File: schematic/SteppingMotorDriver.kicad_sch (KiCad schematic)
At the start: 8 parts

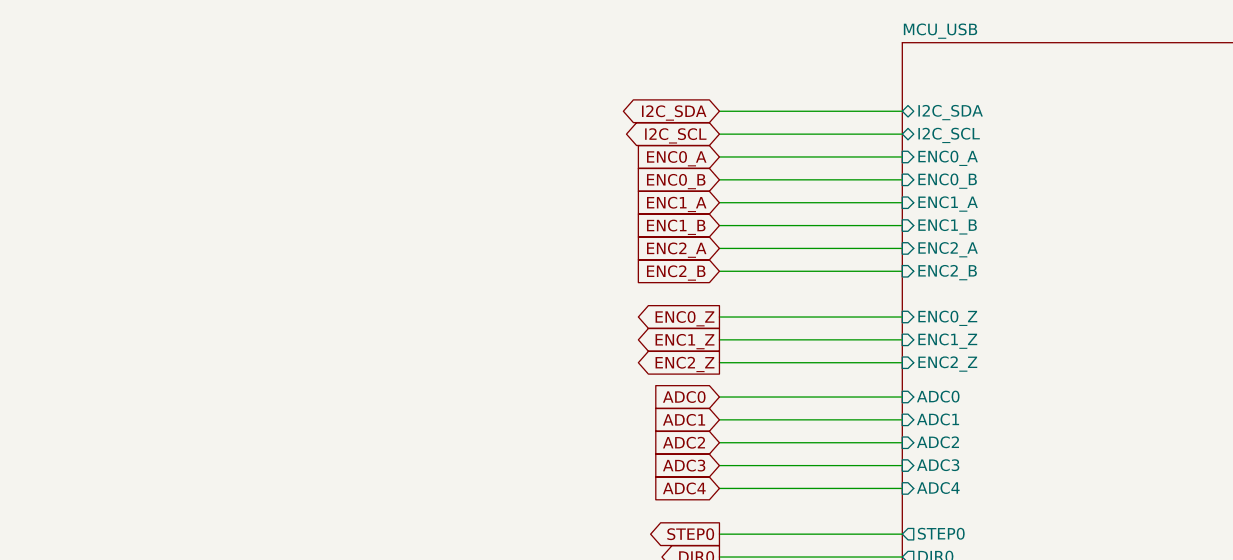
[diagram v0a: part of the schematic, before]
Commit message: Add status LED support, Multiplexer schematic, and Gerber export
Adds status_led.c/h for GPIO46/47 LED indicators, a Multiplexer
schematic sheet, exported Gerber fabrication files, and BLE Codex
prompt docs. Removes stale KiCad auto-backup zips.
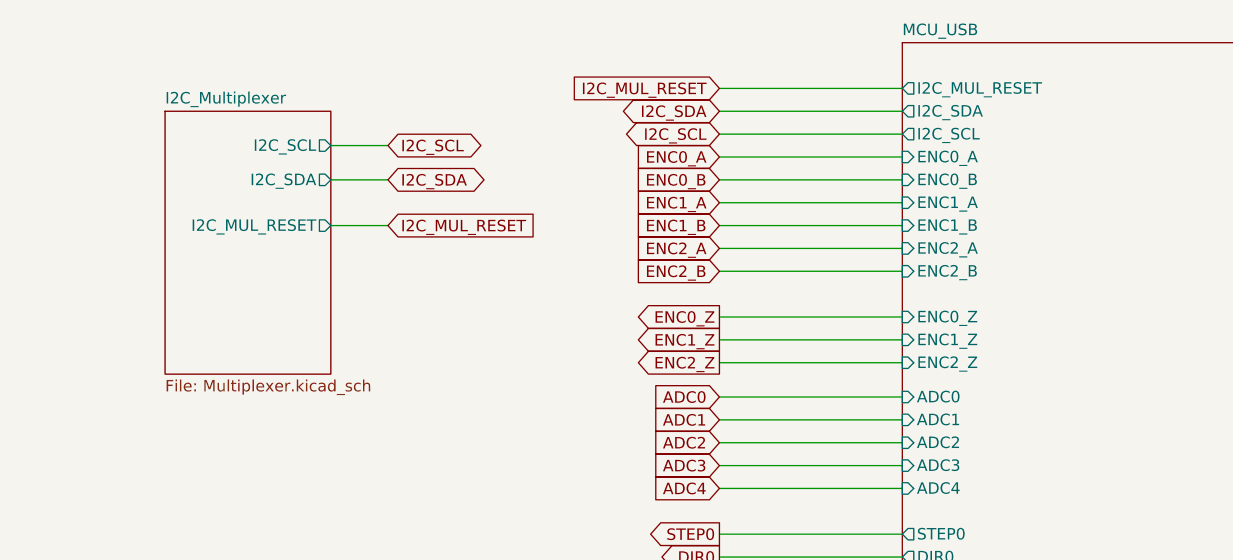
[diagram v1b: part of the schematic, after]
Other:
- added sheet I2C_Multiplexer (Multiplexer.kicad_sch)
- sheet MCU_USB ports: added I2C_MUL_RESET; removed none
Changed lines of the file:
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@@
 	(wire
 		(pts
+			(xy 142.24 31.75) (xy 148.59 31.75)
+		)
+		(stroke
+			(width 0)
+			(type default)
+		)
+	)
+	(wire
+		(pts
 			(xy 201.93 118.11) (xy 217.17 118.11)
 		)
@@
 	(wire
 		(pts
+			(xy 185.42 25.4) (xy 205.74 25.4)
+		)
+		(stroke
+			(width 0)
+			(type default)
+		)
+	)
+	(wire
+		(pts
 			(xy 66.04 62.23) (xy 78.74 62.23)
 		)
@@
 	(wire
 		(pts
+			(xy 142.24 35.56) (xy 148.59 35.56)
+		)
+		(stroke
+			(width 0)
+			(type default)
+		)
+	)
+	(wire
+		(pts
+			(xy 142.24 40.64) (xy 148.59 40.64)
+		)
+		(stroke
+			(width 0)
+			(type default)
+		)
+	)
+	(wire
+		(pts
 			(xy 185.42 33.02) (xy 205.74 33.02)
 		)
@@
 		)
 	)
+	(global_label "I2C_SDA"
+		(shape bidirectional)
+		(at 148.59 35.56 0)
+		(effects
+			(font
+				(size 1.27 1.27)
+			)
+			(justify left)
+		)
+		(property "Intersheetrefs" "${INTERSHEET_REFS}"
+			(at 148.59 35.56 0)
+			(hide yes)
+			(show_name yes)
+			(do_not_autoplace no)
+			(effects
+				(font
+					(size 1.27 1.27)
+				)
+			)
+		)
+	)
+	(global_label "I2C_MUL_RESET"
+		(shape input)
+		(at 148.59 40.64 0)
+		(effects
+			(font
+				(size 1.27 1.27)
+			)
+			(justify left)
+		)
+		(property "Intersheetrefs" "${INTERSHEET_REFS}"
+			(at 148.59 40.64 0)
+			(hide yes)
+			(show_name yes)
+			(do_not_autoplace no)
+			(effects
+				(font
+					(size 1.27 1.27)
+				)
+			)
+		)
+	)
 	(global_label "I2C_SCL"
 		(shape bidirectional)
@@
 		)
 	)
+	(global_label "I2C_MUL_RESET"
+		(shape input)
+		(at 185.42 25.4 180)
+		(effects
+			(font
+				(size 1.27 1.27)
+			)
+			(justify right)
+		)
+		(property "Intersheetrefs" "${INTERSHEET_REFS}"
+			(at 185.42 25.4 0)
+			(hide yes)
+			(show_name yes)
+			(do_not_autoplace no)
+			(effects
+				(font
+					(size 1.27 1.27)
+				)
+			)
+		)
+	)
 	(global_label "ADC1"
 		(shape input)
@@
 		)
 	)
+	(global_label "I2C_SCL"
+		(shape bidirectional)
+		(at 148.59 31.75 0)
+		(effects
+			(font
+				(size 1.27 1.27)
+			)
+			(justify left)
+		)
+		(property "Intersheetrefs" "${INTERSHEET_REFS}"
+			(at 148.59 31.75 0)
+			(hide yes)
+			(show_name yes)
+			(do_not_autoplace no)
+			(effects
+				(font
+					(size 1.27 1.27)
+				)
+			)
+		)
+	)
 	(global_label "ADC1"
 		(shape output)
@@
 			)
 		)
-		(pin "I2C_SDA" bidirectional
+		(pin "I2C_SDA" output
 			(at 205.74 27.94 180)
 			(effects
@@
 			)
 		)
-		(pin "I2C_SCL" bidirectional
+		(pin "I2C_SCL" output
 			(at 205.74 30.48 180)
 			(effects
@@
 			)
 		)
+		(pin "I2C_MUL_RESET" output
+			(at 205.74 25.4 180)
+			(effects
+				(font
+					(size 1.27 1.27)
+				)
+				(justify left)
+			)
+		)
+	)
+	(sheet
+		(at 123.825 27.94)
+		(size 18.415 29.21)
+		(exclude_from_sim no)
+		(in_bom yes)
+		(on_board yes)
+		(dnp no)
+		(fields_autoplaced yes)
+		(stroke
+			(width 0.1524)
+			(type solid)
+		)
+		(fill
+			(color 0 0 0 0)
+		)
+		(property "Sheetname" "I2C_Multiplexer"
+			(at 123.825 27.2284 0)
+			(show_name no)
+			(do_not_autoplace no)
+			(effects
+				(font
+					(size 1.27 1.27)
+				)
+				(justify left bottom)
+			)
+		)
+		(property "Sheetfile" "Multiplexer.kicad_sch"
+			(at 123.825 57.7346 0)
+			(show_name no)
+			(do_not_autoplace no)
+			(effects
+				(font
+					(size 1.27 1.27)
+				)
+				(justify left top)
+			)
+		)
+		(pin "I2C_SCL" output
+			(at 142.24 31.75 0)
+			(effects
+				(font
+					(size 1.27 1.27)
+				)
+				(justify right)
+			)
+		)
+		(pin "I2C_SDA" output
+			(at 142.24 35.56 0)
+			(effects
+				(font
+					(size 1.27 1.27)
+				)
+				(justify right)
+			)
+		)
+		(pin "I2C_MUL_RESET" output
+			(at 142.24 40.64 0)
+			(effects
+				(font
+					(size 1.27 1.27)
+				)
+				(justify right)
+			)
+		)
+		(instances
+			(project "SteppingMotorDriver"
+				(path "/9b845d9c-42fa-43ff-8aea-dde971ea3cf9"
+					(page "2")
+				)
+			)
+		)
